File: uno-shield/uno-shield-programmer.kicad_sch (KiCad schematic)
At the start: 13 parts, among them J1 Power, J2 Digital/PWM, J3 Analog, J4 Digital/PWM, J5 Conn_01x04_Female, J6 Conn_01x04_Female, U1 ATtiny85-20P

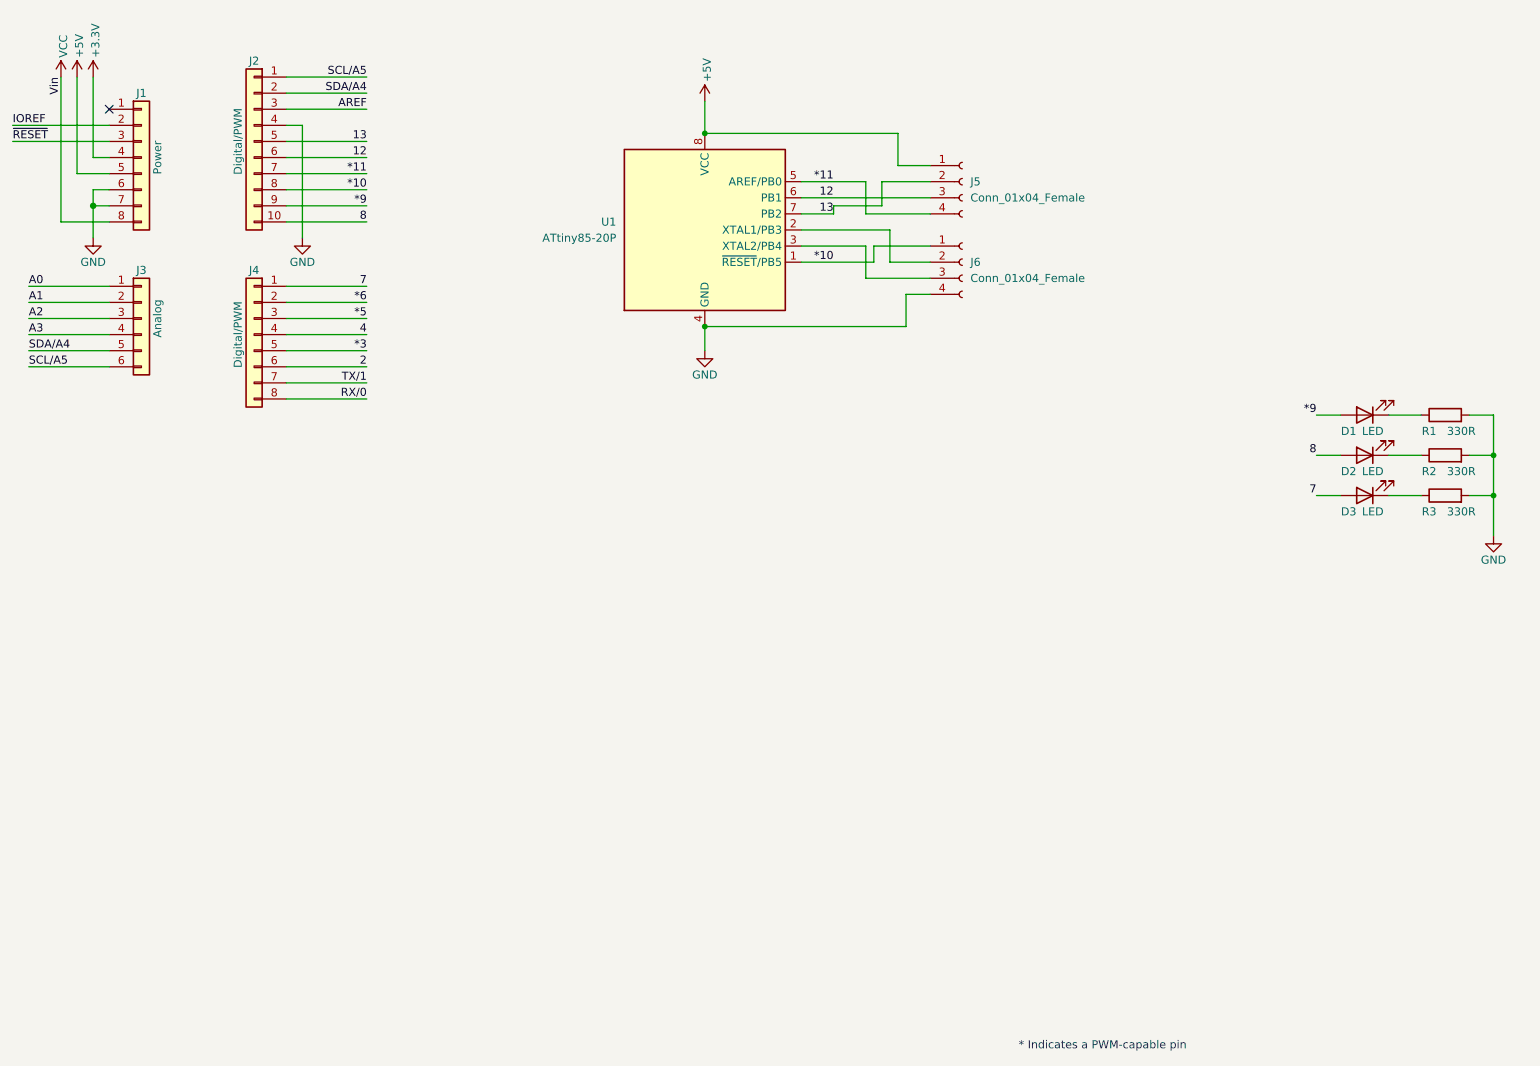
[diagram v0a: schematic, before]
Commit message: move stuff to uno-specific project, add 10uF cap, change to 0603 instead of 0402
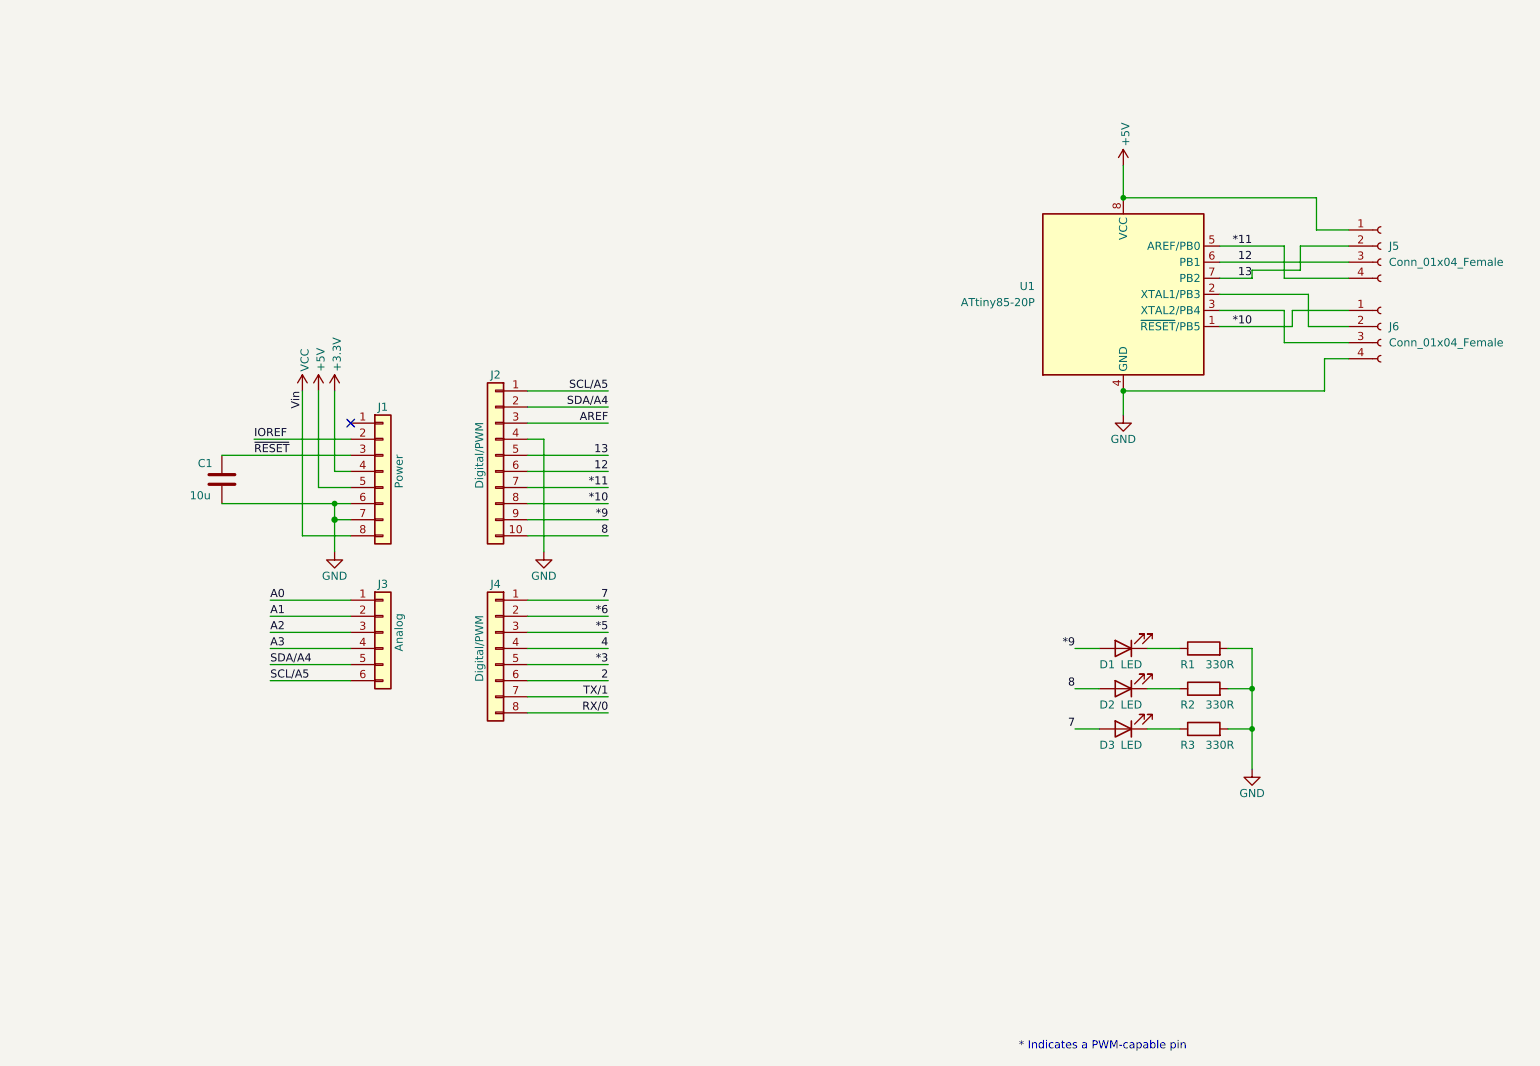
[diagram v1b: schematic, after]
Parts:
- added C1: 10u, Capacitor_SMD:C_0603_1608Metric, symbol Device:C
- D1, D2, D3: footprint LED_SMD:LED_0402_1005Metric -> LED_SMD:LED_0603_1608Metric
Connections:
- net GND: now also C1.2
- net ~{RESET}: now also C1.1
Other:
- moved on the sheet: D1, D2, D3, J1, J2, J3, J4, J5, J6, R1, R2, R3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
